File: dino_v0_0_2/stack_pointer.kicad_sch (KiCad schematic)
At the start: 14 parts, among them U63 74LS169, U64 74LS169, U65 74LS169, U66 74LS169, U67 74LS245, U68 74LS245, U69 74LS08

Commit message: feat: phase C on silicon — CALL and RET execute
The whole ISA now runs on hardware except LDCI and NOP, and those are
microcode-soft rather than missing silicon: C is write-only (RET's scratch)
and nothing can read it back. MOV A,C or PUSHC/POPC retires them for one
three-ROM burn.

    calladdr 0x5C   callraw 0x2A   call 0x4B   stack 0x27

PHASE C COST NO ROM BURN. CALL 0x33 and RET 0x34 were already in the
sockets -- decoded out of roms/U9.bin+U15.bin+U23.bin, 12 and 14 rows, zero
differing from the generator. It was two '245s and wire.

THE FAULT WAS A WRONG TAP, NOT A WRONG WIRE. U72/U73 first went onto
U11/U12 -- the PC LOAD path, whose B side is PCD0-15 feeding the counters'
DATA inputs. CALL needs to READ the PC, so they belong on PC0-15, the Q
outputs, paralleling U13/U14. The schematic said so all along and so did
--continuity; the wiring diverged from a correct list.

Three new images, and the split between them is the point:

  calladdr  CALL without RET. Reads the pushed return address back by
            ABSOLUTE address, so it covers the CALL-side pins (U70.12/.13,
            U72, U73) and none of the RET-side ones (U28.10, U29.11,
            U30.12). Without the split, a failure lights up five pins that
            had never been asserted in this machine's life and names none.
  callraw   REPORTS the pushed byte instead of judging it. This is what
            actually found the fault: calladdr had answered 0xC1 and my
            fault dictionary editorialised that into "-> U72", a healthy
            part. The raw byte was 0x26 -- the previous JMP's target --
            which named stale PCD immediately. An assertion collapses a
            number into a verdict, and the number was the clue. Pair every
            assert-style witness with a raw-report twin when the observable
            is an address or a pointer.
  call      the RETURN ADDRESS as the observable. pads, for RET.

PROG_stack gains a POISON prefix, so its CRC moves 0x9C53 -> 0x1A77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
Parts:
- added R2: 100Ω, symbol Device:R_Small
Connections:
- net CLK: now also R2.1; no longer U63.2 (CP), U64.2 (CP), U65.2 (CP), U66.2 (CP)
- new net CLK_R: R2.2, U63.2 (CP), U64.2 (CP), U65.2 (CP), U66.2 (CP)
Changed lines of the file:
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@@
+	(wire
+		(pts
+			(xy 31.75 90.17) (xy 34.29 90.17)
+		)
+		(stroke
+			(width 0)
+			(type default)
+		)
+	)
 	(wire
 		(pts
@@
 		(pts
 			(xy 228.6 55.88) (xy 229.87 55.88)
+		)
+		(stroke
+			(width 0)
+			(type default)
+		)
+	)
+	(wire
+		(pts
+			(xy 41.91 90.17) (xy 39.37 90.17)
 		)
 		(stroke
@@
 		)
 	)
-	(label "CLK"
+	(label "CLK_R"
 		(at 147.32 135.89 180)
 		(effects
@@
 		)
 	)
-	(label "CLK"
+	(label "CLK_R"
 		(at 87.63 71.12 180)
 		(effects
@@
 		)
 	)
-	(label "CLK"
+	(label "CLK_R"
 		(at 146.05 71.12 180)
 		(effects
@@
 		)
 	)
+	(label "CLK"
+		(at 31.75 90.17 180)
+		(effects
+			(font
+				(size 1.27 1.27)
+			)
+			(justify right bottom)
+		)
+	)
 	(label "~{SP_DOWN}"
 		(at 31.75 115.57 180)
@@
 		)
 	)
+	(label "CLK_R"
+		(at 41.91 90.17 0)
+		(effects
+			(font
+				(size 1.27 1.27)
+			)
+			(justify left bottom)
+		)
+	)
 	(label "~{SP_CE}"
 		(at 87.63 66.04 180)
@@
 		)
 	)
-	(label "CLK"
+	(label "CLK_R"
 		(at 87.63 135.89 180)
 		(effects
@@
 					(unit 1)
 				)
+			)
+		)
+	)
+	(symbol
+		(lib_id "Device:R_Small")
+		(at 36.83 90.17 90)
+		(unit 1)
+		(body_style 1)
+		(exclude_from_sim no)
+		(in_bom yes)
+		(on_board yes)
+		(in_pos_files yes)
+		(dnp no)
+		(fields_autoplaced yes)
+		(property "Reference" "R2"
+			(at 36.83 85.09 90)
+			(show_name no)
+			(do_not_autoplace no)
+			(effects
+				(font
+					(size 1.016 1.016)
+				)
+			)
+		)
+		(property "Value" "100Ω"
+			(at 36.83 87.63 90)
+			(show_name no)
+			(do_not_autoplace no)
+			(effects
+				(font
+					(size 1.27 1.27)
+				)
+			)
+		)
+		(property "Footprint" ""
+			(at 36.83 90.17 0)
+			(hide yes)
+			(show_name no)
+			(do_not_autoplace no)
+			(effects
+				(font
+					(size 1.27 1.27)
+				)
+			)
+		)
+		(property "Datasheet" ""
+			(at 36.83 90.17 0)
+			(hide yes)
+			(show_name no)
+			(do_not_autoplace no)
+			(effects
+				(font
+					(size 1.27 1.27)
+				)
+			)
+		)
+		(property "Description" "Resistor, small symbol"
+			(at 36.83 90.17 0)
+			(hide yes)
+			(show_name no)
+			(do_not_autoplace no)
+			(effects
+				(font
+					(size 1.27 1.27)
+				)
+			)
+		)
+		(pin "1"
+		)
+		(pin "2"
+		)
+		(instances
+			(project "dino_v0_0_2"
+				(path "/e43166a5-d972-471d-b3cf-9f4f12c7f541/24261abe-cc51-4721-a517-eb214e9b8f63"
+					(reference "R2")
+					(unit 1)
+				)

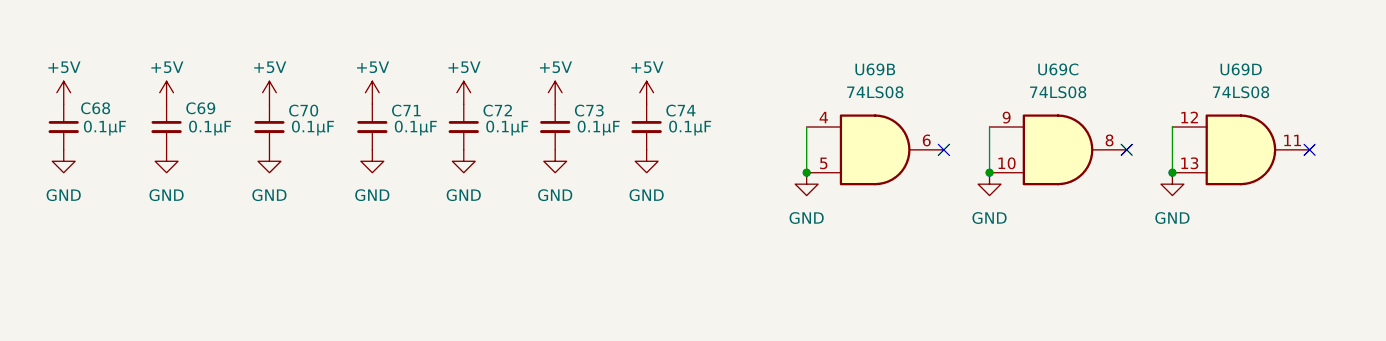
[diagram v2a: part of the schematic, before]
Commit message: feat: phase D on silicon — the machine executes from RAM
PROG_ramexec returns 0x6E. The PC has been above 0x7FFF and FETCH_RAM has
been high, both for the first time in this machine's life.

The missing condition was never "is this a fetch." ~ROM_OUT is asserted for
every src=ROM — opcode fetch, LDAI's immediate, LDA/STA/JMP/CALL operand
bytes — so an instruction living in RAM must read its operands from RAM
too. The condition is "a ROM-side read was requested, but the address is
above 0x7FFF":

    FETCH_RAM = NOR(~ROM_OUT, ~RAM_EN)

Six gate sections, no new IC. All six were free on U22/U37/U39, already in
sockets on the MDR board, where ~ROM_OUT and ~RAM_OUT already sit feeding
READS_IDLE. Only ~RAM_EN had to be brought in.

    U22 g3   FETCH_RAM     = NOR(~ROM_OUT, ~RAM_EN)
    U22 g4   ROM_BUF_ON    = NOR(~ROM_OUT, FETCH_RAM)
    U37 inv4 ~{FETCH_RAM}
    U37 inv6 ~{ROM_BUF_EN} = OR(~ROM_OUT, FETCH_RAM)   -> U19.19
    U37 inv5 ~{RAM_OE_G}   = AND(~RAM_OUT, ~FETCH_RAM) -> U26.22 + U51.9
    U39 g4   RAM_OE_ON     = NAND(~RAM_OUT, ~FETCH_RAM)

Two pin lifts on the memory board, eleven wires. U24.22 stays on ~ROM_OUT:
U24's own ~CE = M15 already deselects the ROM chip at RAM addresses.

Gating ~RAM_OUT upstream is what keeps this at six gates rather than eight.
U51 is a 7400 computing ~RAM_MDR_EN = AND(~RAM_OUT, ~WRITE_DIR), so one
gate on ~RAM_OUT moves both the RAM chip's ~OE and its buffer's ~CE.

Re-proved before building: all 15 src=ROM microcode rows carry mux_pc=True,
FETCH included, and FILL is src=NONE. A ROM-side read can now land in RAM,
so the standing "ROM reads are exempt from the src=RAM -> MAR loop" rule was
no longer free. It holds — MAR never drives M during a ROM-side read, and a
runaway opcode cannot open the loop either.

The witness is not permutation-blind. If the fetch had still come from ROM,
PC=0x9000 presents A0-A14 = 0x1000 to U24, which is 0xFF fill, which is
HALT, so the poison would have survived as 0xFF. 0x6E is 0x8B - 0x1D,
compu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
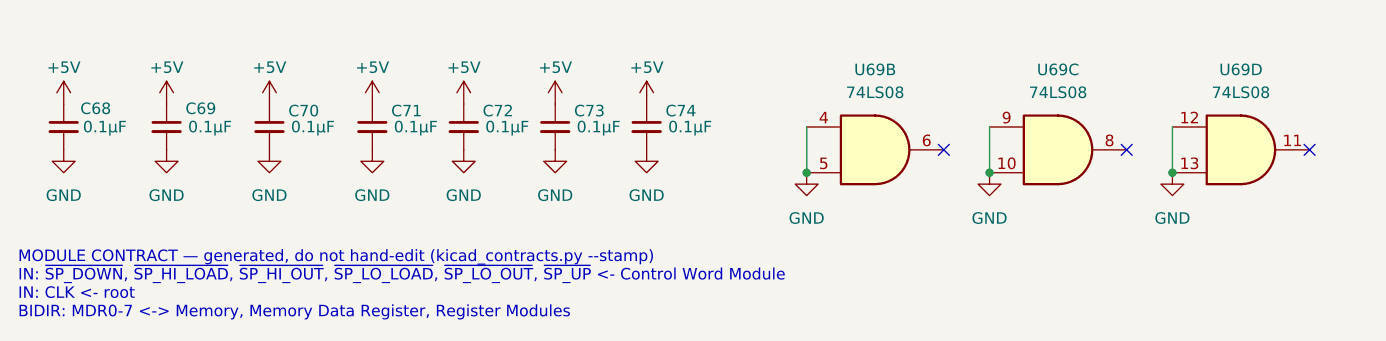
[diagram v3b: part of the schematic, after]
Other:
- note added: "MODULE CONTRACT — generated, do not hand-edit (kicad_contracts.py --stamp) IN: ~{SP_DOWN}, ~{SP_HI_LOAD}, ~{SP_HI_OUT}, ~{SP_LO_LOAD}, ~{SP_LO_OUT}, ~{SP_UP} <- Control Word Module IN: CLK <- root BIDIR: MDR0-7 <-> Memory, Memory Data Register, Register Modules"
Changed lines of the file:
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@@
+		)
+	)
+	(text "MODULE CONTRACT — generated, do not hand-edit (kicad_contracts.py --stamp)\nIN: ~{SP_DOWN}, ~{SP_HI_LOAD}, ~{SP_HI_OUT}, ~{SP_LO_LOAD}, ~{SP_LO_OUT}, ~{SP_UP} <- Control Word Module\nIN: CLK <- root\nBIDIR: MDR0-7 <-> Memory, Memory Data Register, Register Modules"
+		(exclude_from_sim no)
+		(at 15.24 206.85 0)
+		(effects
+			(font
+				(size 1.27 1.27)
+			)
+			(justify left bottom)
 		)
 	)

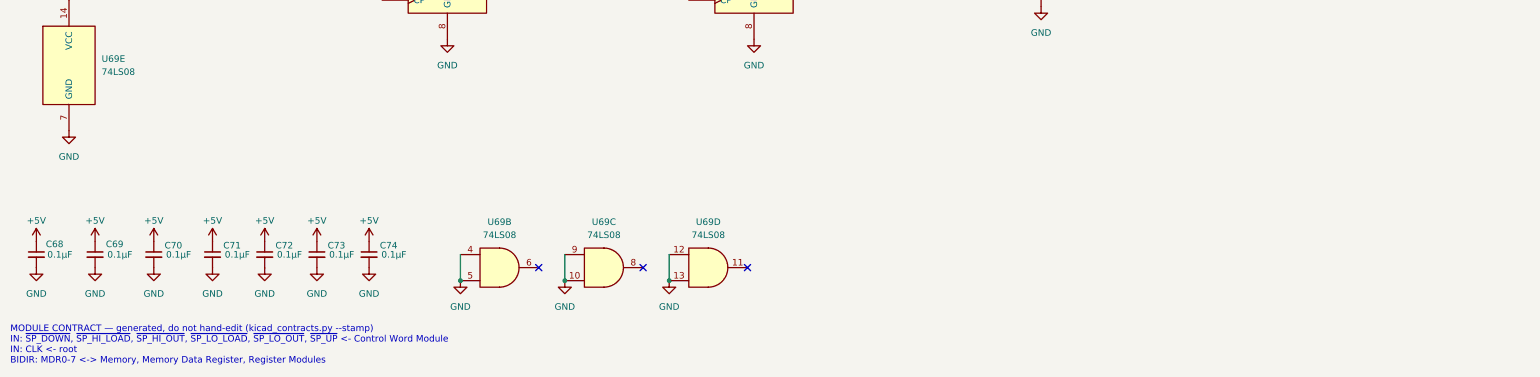
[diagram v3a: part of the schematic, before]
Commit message: feat: phase E step A -- the 16K I/O window, in schematic
Carves 0x4000-0x7FFF out of ROM space and publishes a bus. The ROM now
answers 0x0000-0x3FFF only; the window decodes to no core chip, so W
reads its park -- 0xFF, which is HALT.

TWO NEW PACKAGES, both on the memory board:

  U74 '00  ~{M14}      = NAND(M14, M14)
           ~{ROM_SEL}  = NAND(~{RAM_EN}, ~{M14})
           ~{RAM_OE_G} = NAND(RAM_OE_ON, M15)
           ~{IO_SEL}   = NAND(~{RAM_EN}, M14)
  U75 '32  ~{IO_RD}    = OR(~{IO_SEL}, READS_IDLE)
           ~{IO_WR}    = OR(~{IO_SEL}, ~{RAM_WRITE_EN})
           RESET_B     = OR(RESET, GND)
           ~{IO_RD_Q}  = OR(~{IO_RD}, CLK)

Eight copper changes: U24.20 and U22.12 to ~{ROM_SEL}, U26.22/U51.9 fed
from U74 g3, U39.10 to ~{IO_RD}, U37.10 and U28.7 unlanded, U37.11 to
GND. Park: R4-R8 + R25-R27, 4.7k on W0-7. CLK crosses through R3, 100R,
source end -- the R2 treatment.

IN RETIRES. ~{SW_OUT} has zero pins project-wide. SWITCH-GATE1's enables
are strapped +5V until card zero drives them from an address decode.

THE ROM_EN ALIAS IS DELETED. Once U24.20 moved, ROM_EN named a net with
no ROM consumer. Deleting it half-way SPLIT the net and alias_splits()
caught it mid-edit -- M15: ['M15', 'M15/ROM_EN'], the exact two-key
failure that once cost this project the ROM chip-enable on every
continuity checklist ever generated.

CLK WAS A FOURTH CROSSING THE SPEC DID NOT CARRY. Census: 15 CLK pins,
none on the memory board; ~{CLK} at U51.4 is the wrong polarity and both
new packages are full. SECTION 1's cost table predated the read-term
split that spent U75 g4, so memory is +4 and MDR is +4 -- the wire margin
is zero. Ruled: stay on memory, the output-load argument still holds.

SWITCH-GATE1/SW1/R17-R24/C48 move to their own input.kicad_sch so the
DIP card is modelled as a card. No renumbering: 168 designators
unchanged, --since reports annotate=0.

TOOLING RECONCILED TO THE DESIGN, not the reverse:
  test_continuity_completeness  M15_PINS U24.20 -> U74.10; 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
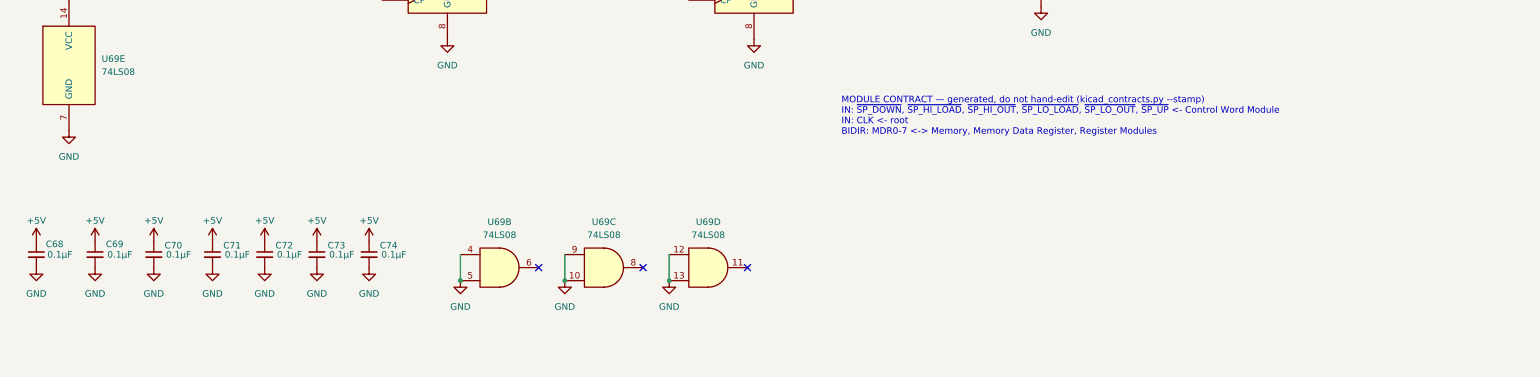
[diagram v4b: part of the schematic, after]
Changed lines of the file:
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@@
 	(text "MODULE CONTRACT — generated, do not hand-edit (kicad_contracts.py --stamp)\nIN: ~{SP_DOWN}, ~{SP_HI_LOAD}, ~{SP_HI_OUT}, ~{SP_LO_LOAD}, ~{SP_LO_OUT}, ~{SP_UP} <- Control Word Module\nIN: CLK <- root\nBIDIR: MDR0-7 <-> Memory, Memory Data Register, Register Modules"
 		(exclude_from_sim no)
-		(at 15.24 206.85 0)
+		(at 177.038 162.306 0)
 		(effects
 			(font
